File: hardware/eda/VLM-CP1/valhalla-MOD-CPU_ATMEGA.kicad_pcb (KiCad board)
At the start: 2 copper layers, 76.2 x 81.3 mm, 34 parts, among them J1 GPIO, J2 ICSP, J3 BUS, K1 RESET, U1 ATmega328P-P, U2 74LS06, U3 74LS07, Y1 7.3728 MHz

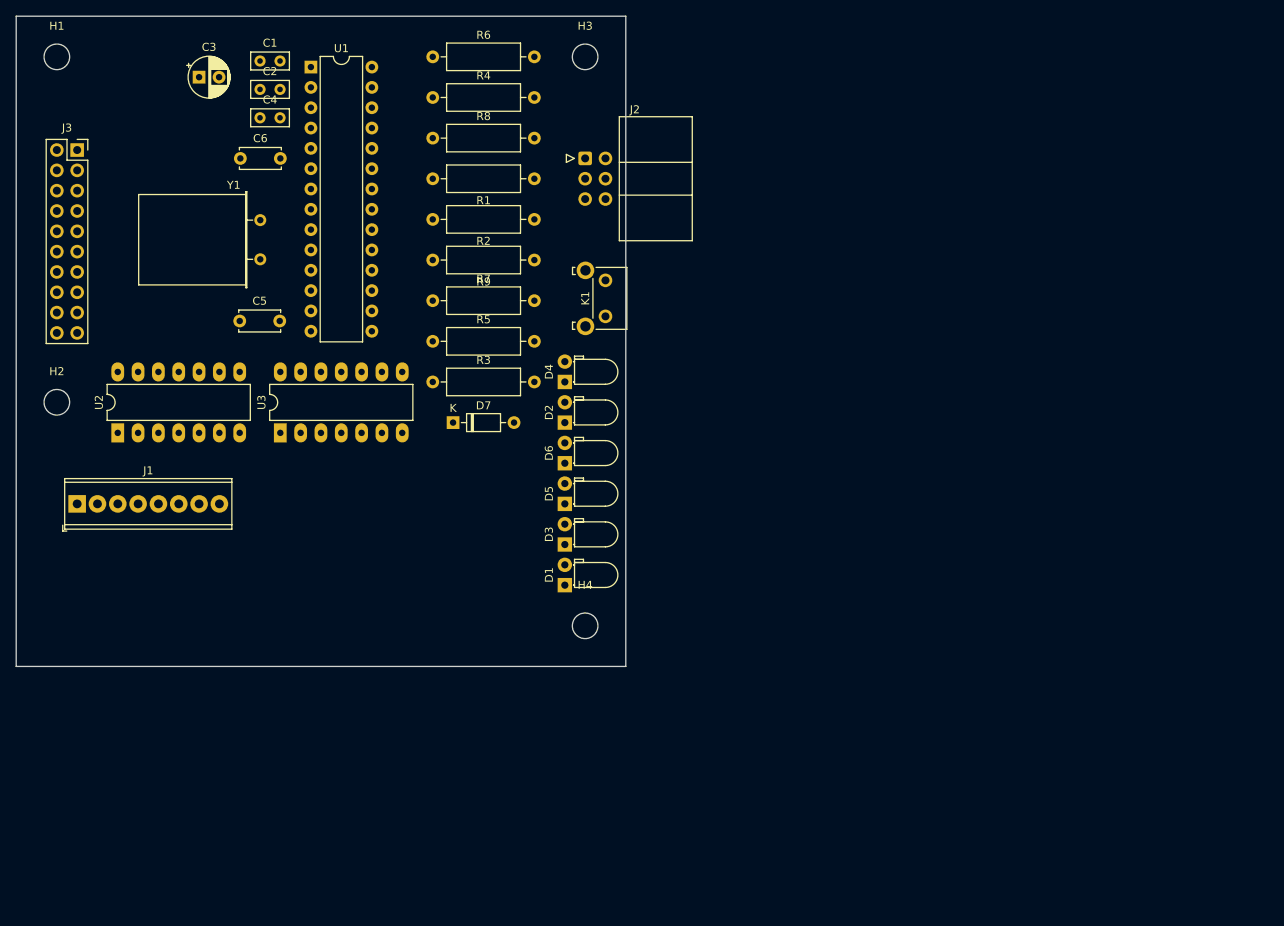
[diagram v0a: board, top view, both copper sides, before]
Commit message: UPDATE: formal dimensions for Valhalla MOD and progrss on CPU
 - added formal dimensions to the Valhalla MOD PSU PCB, to serve as a
   future template and as documentation
 - changed Zener/Schottky symbols to filled variant on same module,
   as customary in the EU
 - solved the Vio independence issue for the UI LEDs on the CPU module
   with a switchable regulator
 - finalized canonical dimensions of the CPU module and placed UI
   LEDs in two rows.
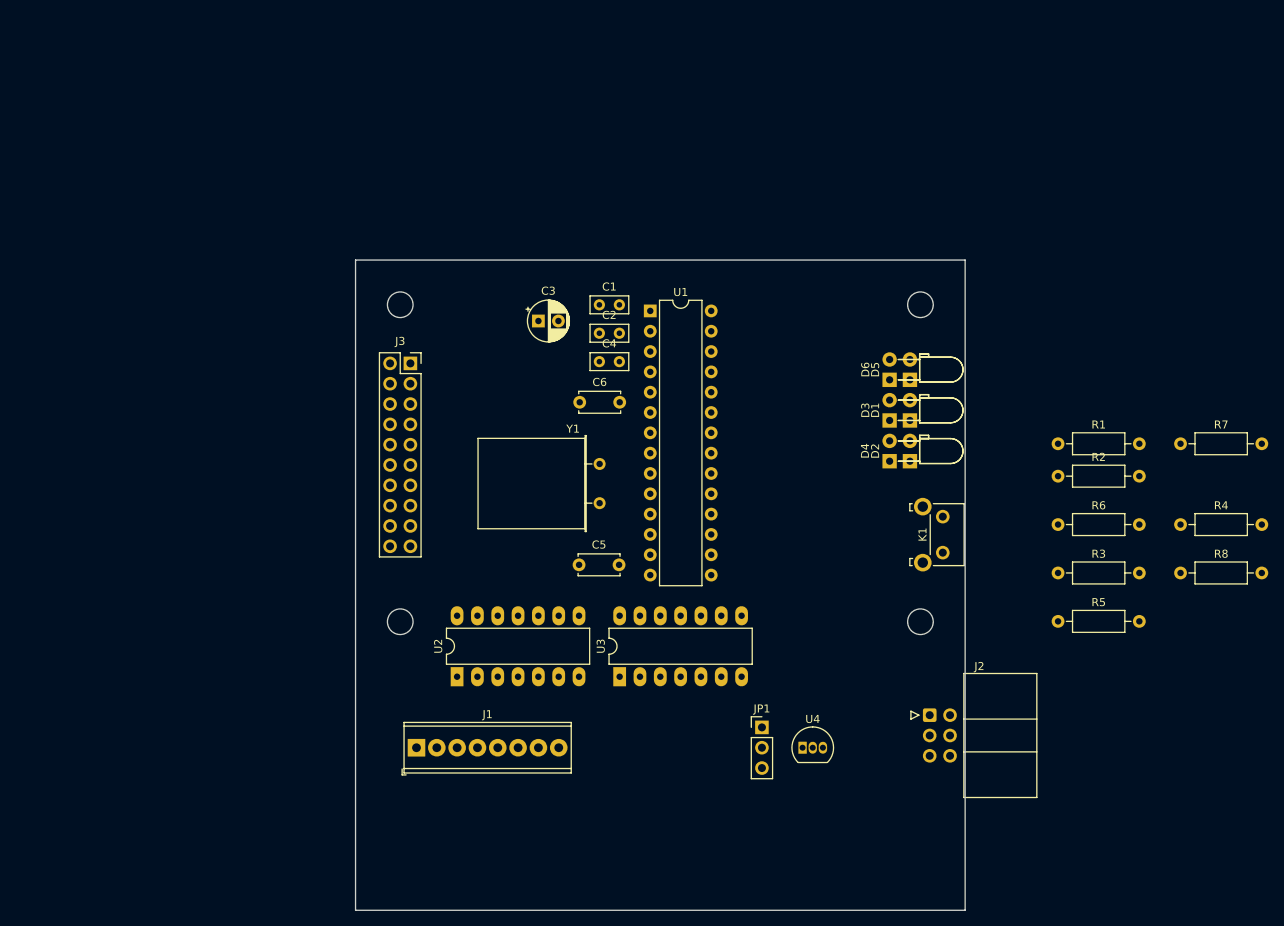
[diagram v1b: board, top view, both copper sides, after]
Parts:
- removed D7: 3.3V, Diode_THT:D_DO-35_SOD27_P7.62mm_Horizontal
- removed R9: *1, Resistor_THT:R_Axial_DIN0309_L9.0mm_D3.2mm_P12.70mm_Horizontal
- added JP1: LED_VCC, Connector_PinHeader_2.54mm:PinHeader_1x03_P2.54mm_Vertical, F.Cu at (144.0, 114.3)
- added U4: L78L33_TO92, Package_TO_SOT_THT:TO-92_Inline, F.Cu at (149.1, 116.8)
- D3, D4, D6: footprint LED_THT:LED_D3.0mm_Horizontal_O1.27mm_Z2.0mm -> LED_THT:LED_D3.0mm_Horizontal_O3.81mm_Z6.0mm
- R1, R2, R3, R4, R5, R6, R7, R8: footprint Resistor_THT:R_Axial_DIN0309_L9.0mm_D3.2mm_P12.70mm_Horizontal -> Resistor_THT:R_Axial_DIN0207_L6.3mm_D2.5mm_P10.16mm_Horizontal
- moved R8 108.1 mm to (196.3, 95.0)
- moved R4 107.6 mm to (196.3, 88.9)
- moved R6 97.6 mm to (181.0, 88.9)
- moved R7 95.2 mm to (196.3, 78.8)
- moved R5 85.6 mm to (181.0, 101.0)
- moved J2 81.8 mm to (165.0, 112.8)
- moved R3 81.7 mm to (181.0, 95.0)
- moved R1 73.4 mm to (181.0, 78.8), turned to 0 degrees
- moved R2 72.9 mm to (181.0, 82.9), turned to 0 degrees
- moved H1 52.9 mm to (98.8, 61.5)
- moved C5 52.2 mm to (121.2, 94.0)
- moved U3 52.2 mm to (126.2, 108.0)
- moved C2 52.2 mm to (123.7, 65.0)
- moved J1 52.2 mm to (100.8, 116.8)
- moved U2 52.2 mm to (105.9, 108.0)
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
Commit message: UPDATE: progress on component placement for CPU module
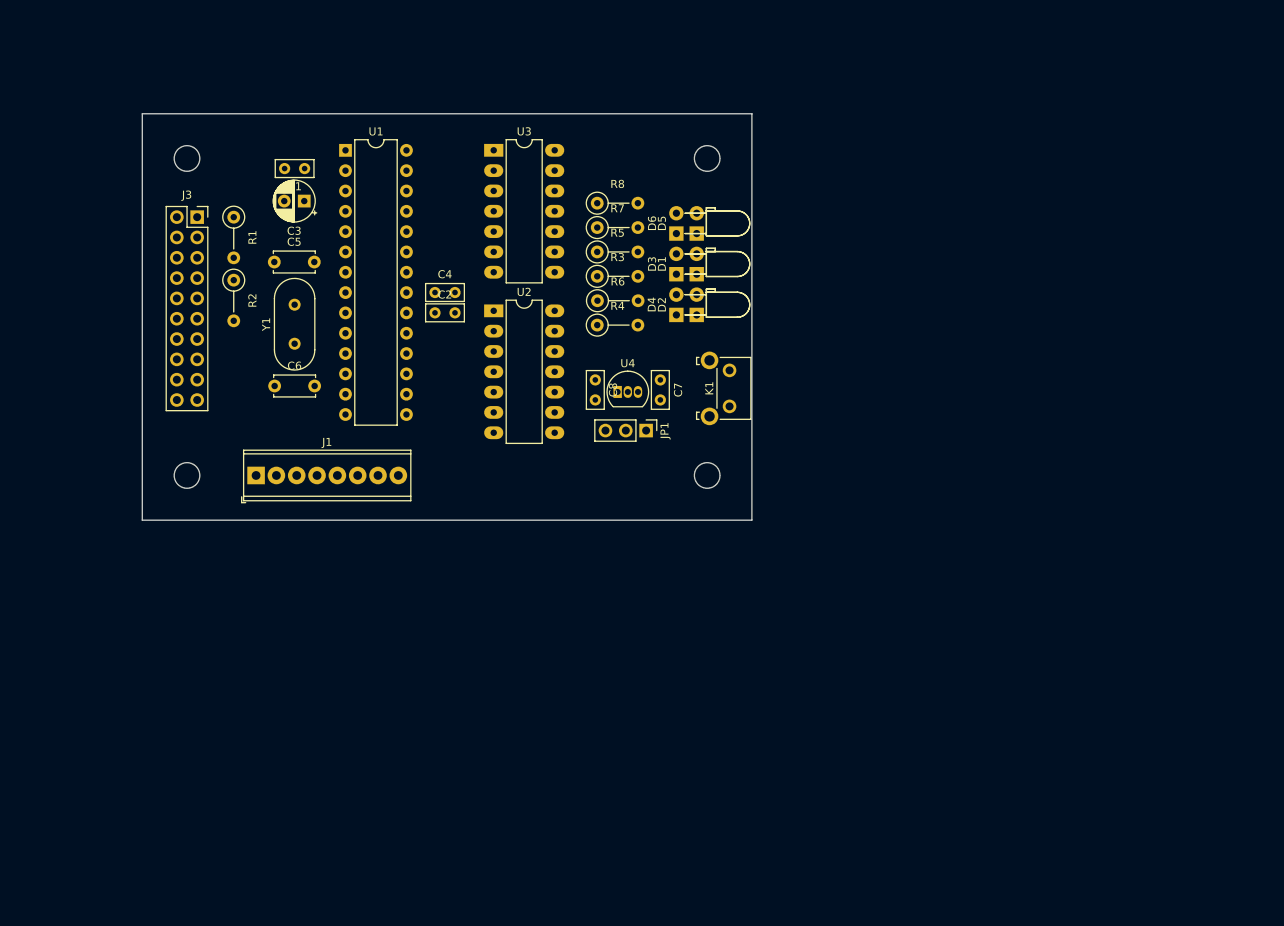
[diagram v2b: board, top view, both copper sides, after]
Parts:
- removed J2: ICSP, Connector_IDC:IDC-Header_2x03_P2.54mm_Horizontal
- added C7: 330nF, Capacitor_THT:C_Rect_L4.6mm_W2.0mm_P2.50mm_MKS02_FKP02, F.Cu at (131.3, 70.9)
- added C8: 0.1uF, Capacitor_THT:C_Rect_L4.6mm_W2.0mm_P2.50mm_MKS02_FKP02, F.Cu at (123.2, 70.9)
- R1, R2, R3, R4, R5, R6, R7, R8: footprint Resistor_THT:R_Axial_DIN0207_L6.3mm_D2.5mm_P10.16mm_Horizontal -> Resistor_THT:R_Axial_DIN0207_L6.3mm_D2.5mm_P5.08mm_Vertical
- Y1: footprint Crystal:Crystal_HC49-U_Horizontal -> Crystal:Crystal_HC49-4H_Vertical
- moved R1 106.9 mm to (78.0, 50.5), turned to -90 degrees
- moved R2 105.9 mm to (78.0, 58.4), turned to -90 degrees
- moved R8 86.3 mm to (123.4, 48.8)
- moved R7 77.8 mm to (123.4, 51.8)
- moved R4 77.1 mm to (123.4, 64.0)
- moved R5 73.8 mm to (123.4, 54.9)
- moved R3 68.5 mm to (123.4, 57.9)
- moved U3 67.7 mm to (110.5, 42.2), turned to 0 degrees
- moved R6 64.0 mm to (123.5, 61.0)
- moved C5 53.7 mm to (83.1, 56.1)
- moved U4 50.1 mm to (126.0, 72.4)
- moved U2 46.0 mm to (110.5, 62.2), turned to 0 degrees
- moved U1 43.1 mm to (92.0, 42.2)
- moved Y1 41.0 mm to (85.6, 66.3), turned to 90 degrees
- moved C1 40.6 mm to (86.9, 44.4), turned to 180 degrees
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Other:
- board size 76.2 x 81.3 mm -> 76.2 x 50.8 mm

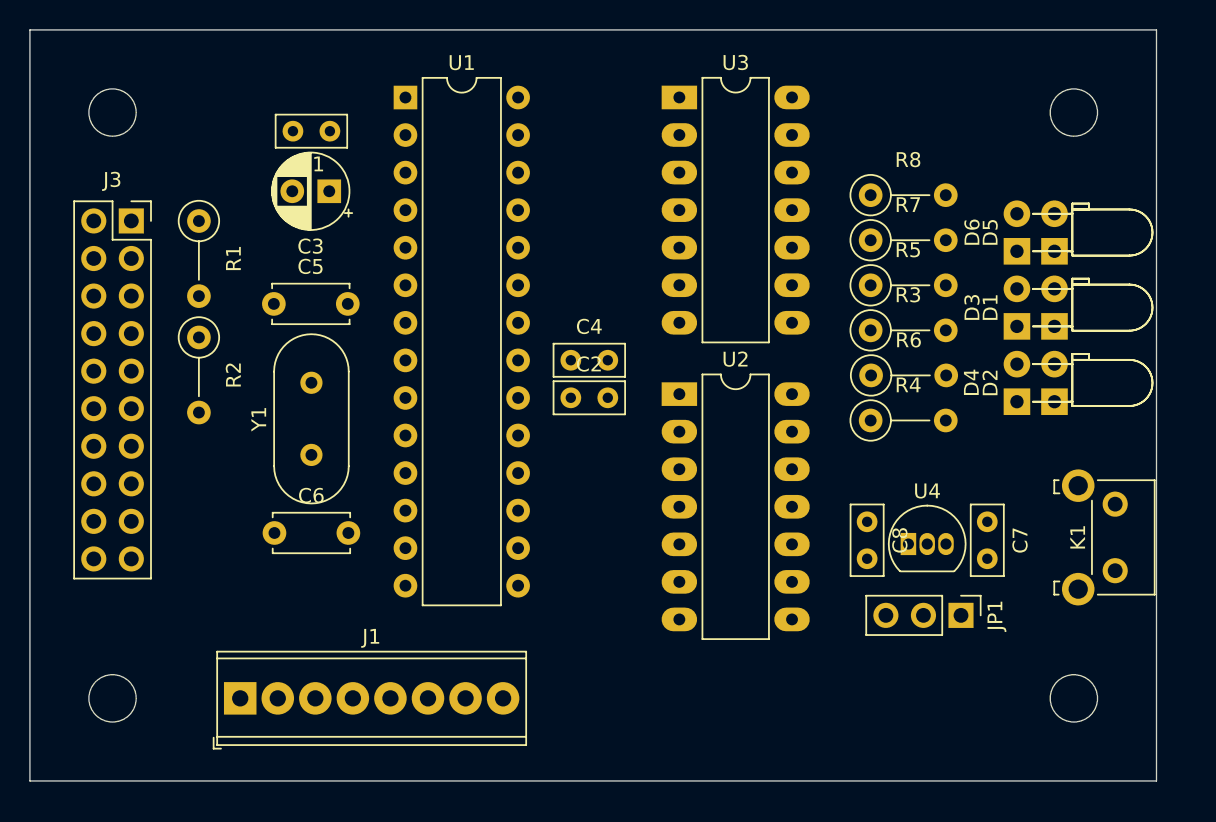
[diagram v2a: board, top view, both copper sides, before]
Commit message: UPDATE: CPU module trace routing complete
 - remaining stuff: crystal dress-up and silkscreen finish-up
 - we may choose not to get artsy on this one (teardrops and curves) due
   to DRC/real estate constraints.
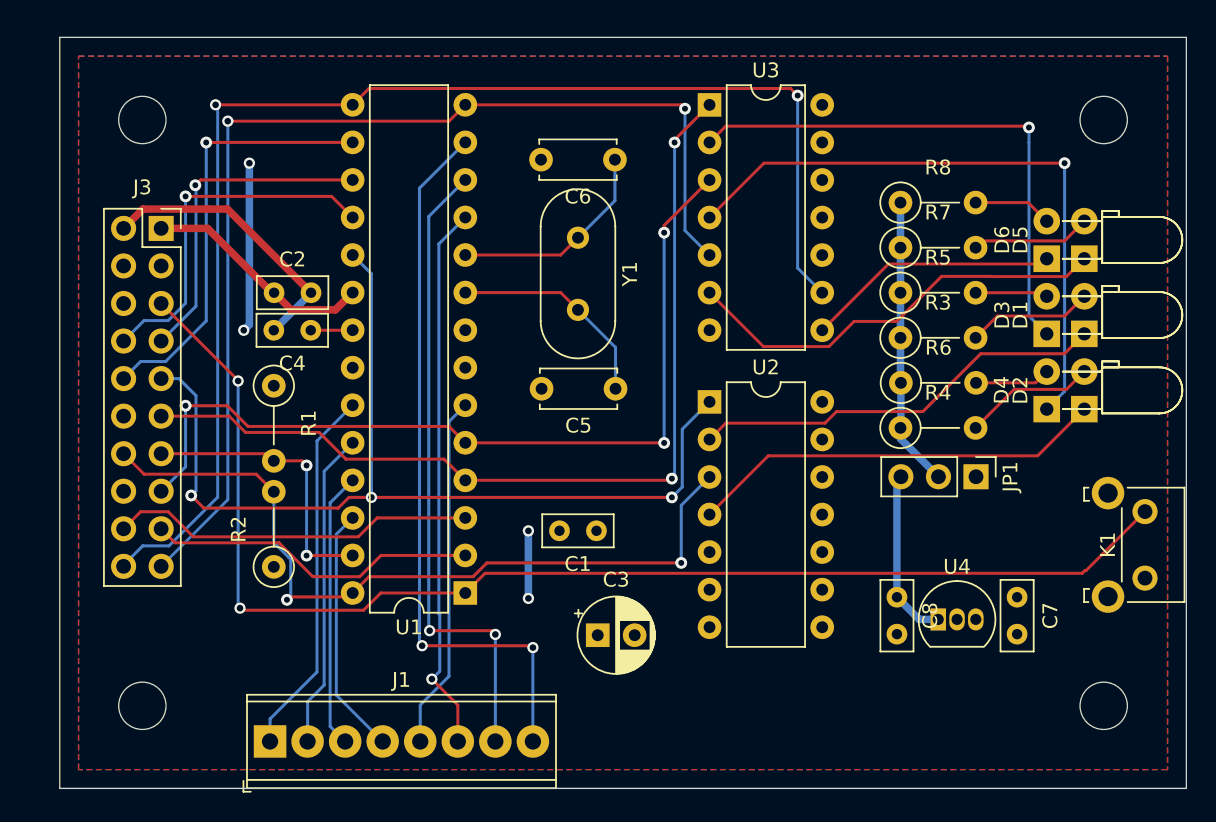
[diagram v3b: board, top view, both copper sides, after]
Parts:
- U2, U3: footprint Package_DIP:DIP-14_W7.62mm_LongPads -> Package_DIP:DIP-14_W7.62mm
- moved C3 35.1 mm to (105.0, 78.5), turned to 0 degrees
- moved C6 34.2 mm to (106.1, 46.4), turned to 180 degrees
- moved U1 33.8 mm to (96.0, 75.7), turned to 180 degrees
- moved C1 32.5 mm to (104.9, 71.5)
- moved C5 23.8 mm to (106.2, 61.9), turned to 180 degrees
- moved Y1 23.3 mm to (103.6, 51.7), turned to -90 degrees
- moved C2 21.3 mm to (83.1, 55.4)
- moved C4 17.7 mm to (85.6, 57.9), turned to 180 degrees
- moved R2 16.3 mm to (83.1, 73.9), turned to 90 degrees
- moved R1 12.2 mm to (83.1, 61.7)
- moved JP1 9.43 mm to (130.6, 67.8)
- moved U4 5.48 mm to (128.0, 77.5)
- moved C7 5.48 mm to (133.3, 76.0)
- moved C8 5.48 mm to (125.2, 76.0)
- moved J1 3.55 mm to (82.8, 85.7)
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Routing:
- net /~{DCD}: track 0.00 -> 89.0 mm, vias 0 -> 2
- net /~{RESET}: track 0.00 -> 86.9 mm, vias 0 -> 2
- net /~{RTS}: track 0.00 -> 74.1 mm, vias 0 -> 2
- net /SCK: track 0.00 -> 67.3 mm, vias 0 -> 3
- net /~{SINT}: track 0.00 -> 62.7 mm, vias 0 -> 2
- net /~{IINT}: track 0.00 -> 58.9 mm, vias 0 -> 3
- net /SCL: track 0.00 -> 53.4 mm, vias 0 -> 2
- net /GPIO7: track 0.00 -> 49.3 mm, vias 0 -> 2
- net /GPIO6: track 0.00 -> 43.3 mm, vias 0 -> 2
- net Net-(D4-K): track 0.00 -> 42.7 mm, vias 0 -> 1
- net /GPIO5: track 0.00 -> 37.2 mm, vias 0 -> 1
- net Net-(D3-K): track 0.00 -> 36.5 mm, vias 0 -> 1
- net Net-(D5-K): track 0.00 -> 29.3 mm
- net /~{SS}: track 0.00 -> 29.2 mm, vias 0 -> 1
- net Net-(D1-K): track 0.00 -> 28.3 mm
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- added copper zone on B.Cu, net /DGND
- added copper zone on F.Cu, net /DVCC

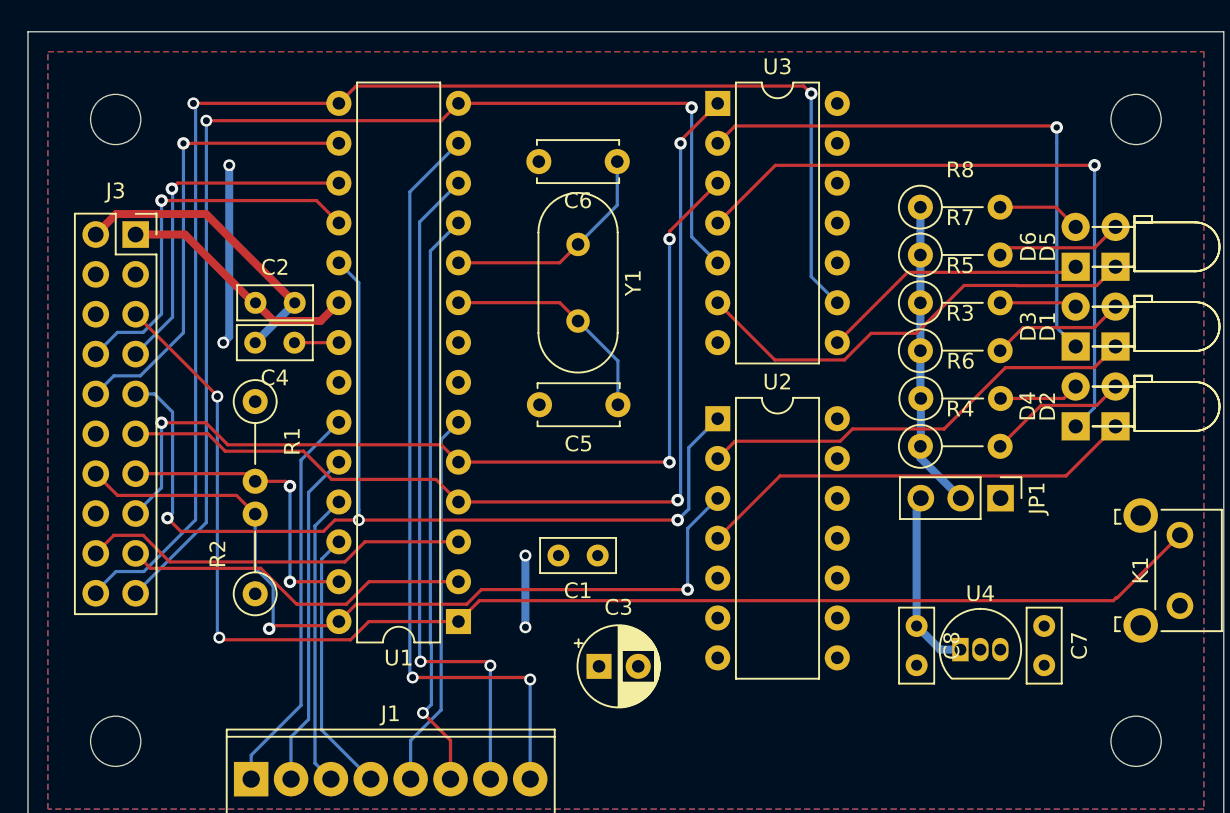
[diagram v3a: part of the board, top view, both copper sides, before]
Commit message: UPDATE: progress towards templatizing dimensions   - used the PSU module as a master copy for now until the template     stabilizes, to be exported as a stand-alone blueprint for future     modules   - minor progress on the CPU(ATMega) module: easier to solder     footprint for LVCC regulator, crystal dress-up and reference     clean-ups.
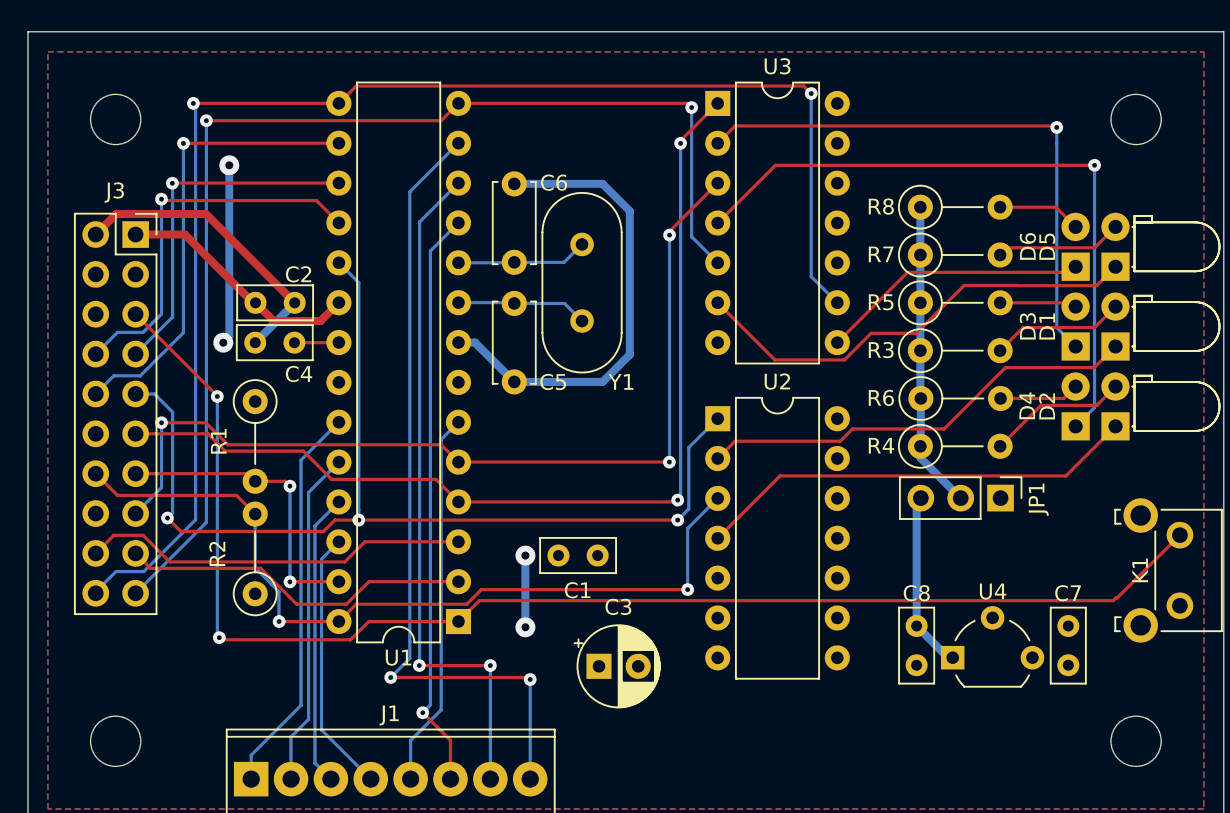
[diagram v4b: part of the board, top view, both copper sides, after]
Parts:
- U4: footprint Package_TO_SOT_THT:TO-92_Inline -> Package_TO_SOT_THT:TO-92_Wide
- moved C5 9.23 mm to (99.6, 55.4), turned to -90 degrees
- moved C6 9.18 mm to (99.6, 52.8), turned to 90 degrees
- moved C7 1.54 mm to (134.9, 76.0)
- moved U4 0.71 mm to (127.5, 78.0)
- moved Y1 0.25 mm to (103.9, 51.7)
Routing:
- net /DGND: track 0.00 -> 29.9 mm
- net Net-(U1-XTAL1/PB6): track 14.5 -> 8.36 mm
- net Net-(U1-XTAL2/PB7): track 14.4 -> 8.36 mm
- net /GPIO7: track 49.3 -> 51.1 mm
- net /SCL: track 53.4 -> 52.6 mm
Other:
- rule pad_to_mask_clearance: 0 -> 0.0508
